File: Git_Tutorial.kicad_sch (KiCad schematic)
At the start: 0 parts

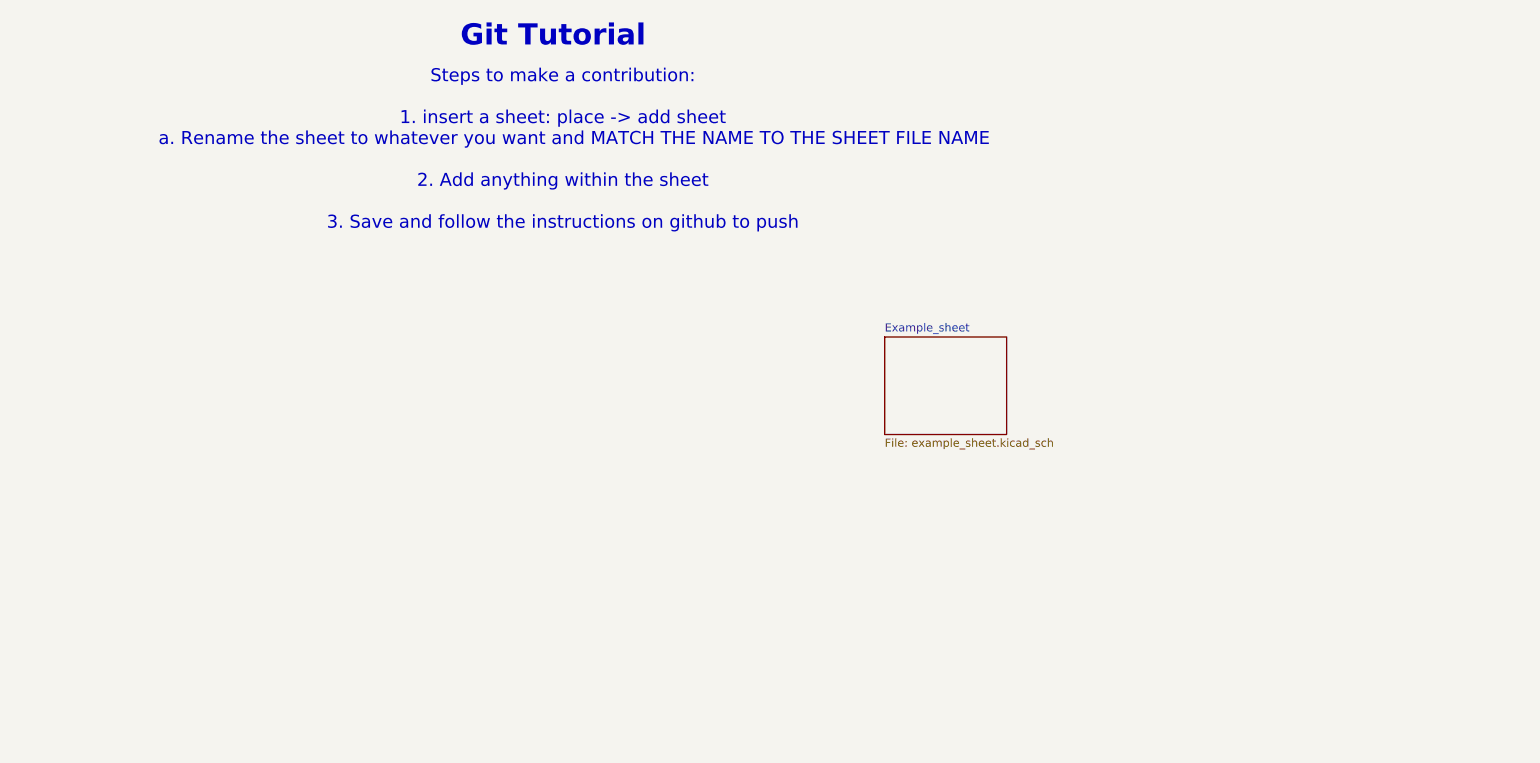
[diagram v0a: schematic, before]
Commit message: new branch text added
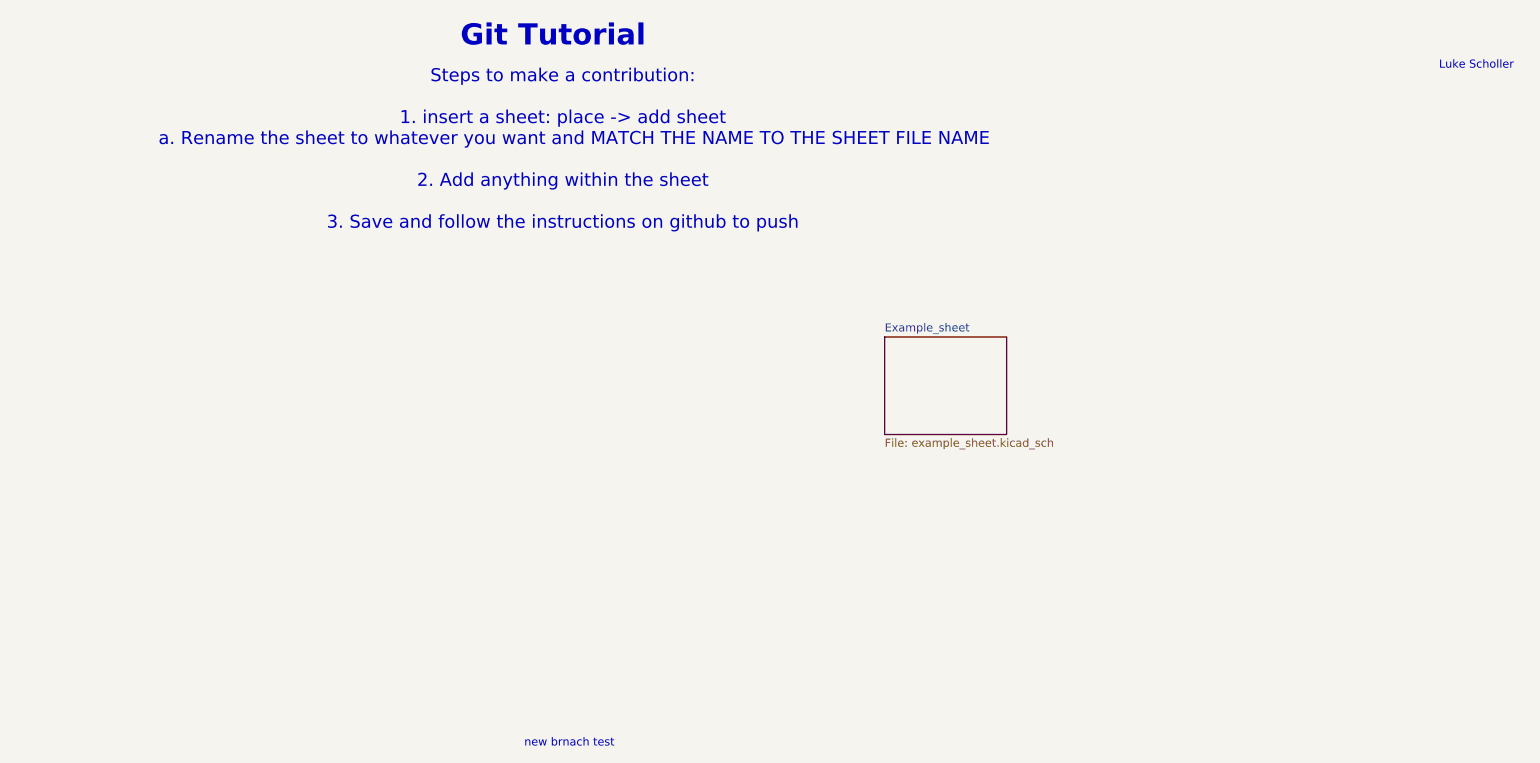
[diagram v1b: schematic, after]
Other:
- note added: "Luke Scholler"
- note added: "new brnach test"
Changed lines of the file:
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@@
 (kicad_sch
-	(version 20231120)
+	(version 20250114)
 	(generator "eeschema")
-	(generator_version "8.0")
+	(generator_version "9.0")
 	(paper "A4")
 	(text "Steps to make a contribution:\n\n1. insert a sheet: place -> add sheet\n	a. Rename the sheet to whatever you want and MATCH THE NAME TO THE SHEET FILE NAME\n\n2. Add anything within the sheet\n\n3. Save and follow the instructions on github to push"
@@
 		)
 	)
+	(text "Luke Scholler"
+		(exclude_from_sim no)
+		(at 229.616 32.512 0)
+		(effects
+			(font
+				(size 1.27 1.27)
+			)
+		)
+	)
+	(text "new brnach test\n"
+		(exclude_from_sim no)
+		(at 87.884 138.43 0)
+		(effects
+			(font
+				(size 1.27 1.27)
+			)
+		)
+	)
 	(sheet
 		(at 137.16 74.93)
 		(size 19.05 15.24)
+		(exclude_from_sim no)
+		(in_bom yes)
+		(on_board yes)
+		(dnp no)
 		(fields_autoplaced yes)
 		(stroke
@@
 		)
 	)
+	(embedded_fonts no)
 )
